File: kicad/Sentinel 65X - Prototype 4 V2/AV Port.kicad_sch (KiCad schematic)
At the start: 10 parts, among them J2 Conn_02x12_Odd_Even

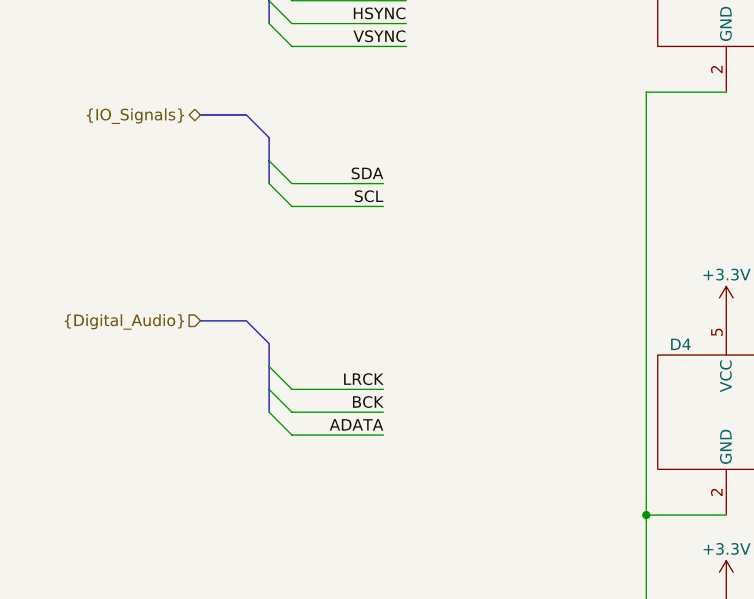
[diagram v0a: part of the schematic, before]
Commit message: Updated prototype 4V2 schematic
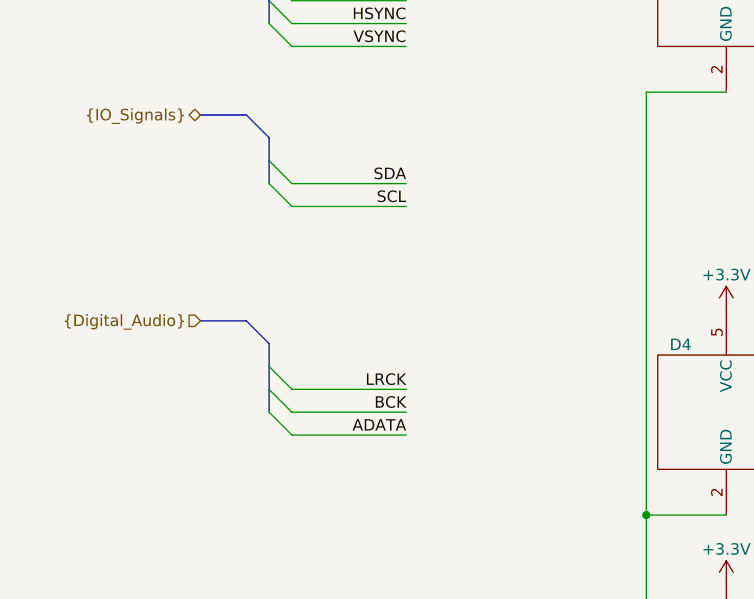
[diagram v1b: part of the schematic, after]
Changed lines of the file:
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@@
 	(wire
 		(pts
-			(xy 55.88 104.14) (xy 66.04 104.14)
+			(xy 55.88 104.14) (xy 68.58 104.14)
 		)
 		(stroke
@@
 	(wire
 		(pts
-			(xy 55.88 76.2) (xy 66.04 76.2)
+			(xy 55.88 76.2) (xy 68.58 76.2)
 		)
 		(stroke
@@
 	(wire
 		(pts
-			(xy 55.88 78.74) (xy 66.04 78.74)
+			(xy 55.88 78.74) (xy 68.58 78.74)
 		)
 		(stroke
@@
 	(wire
 		(pts
-			(xy 55.88 99.06) (xy 66.04 99.06)
+			(xy 55.88 99.06) (xy 68.58 99.06)
 		)
 		(stroke
@@
 	(wire
 		(pts
-			(xy 55.88 101.6) (xy 66.04 101.6)
+			(xy 55.88 101.6) (xy 68.58 101.6)
 		)
 		(stroke
@@
 	)
 	(label "SDA"
-		(at 66.04 76.2 180)
+		(at 68.58 76.2 180)
 		(fields_autoplaced yes)
 		(effects
@@
 	)
 	(label "SCL"
-		(at 66.04 78.74 180)
+		(at 68.58 78.74 180)
 		(fields_autoplaced yes)
 		(effects
@@
 	)
 	(label "ADATA"
-		(at 66.04 104.14 180)
+		(at 68.58 104.14 180)
 		(fields_autoplaced yes)
 		(effects
@@
 	)
 	(label "BCK"
-		(at 66.04 101.6 180)
+		(at 68.58 101.6 180)
 		(fields_autoplaced yes)
 		(effects
@@
 	)
 	(label "LRCK"
-		(at 66.04 99.06 180)
-		(fields_autoplaced yes)
-		(effects
+		(at 68.58 99.06 180)
+		(fields_autoplaced yes)
+		(effects
